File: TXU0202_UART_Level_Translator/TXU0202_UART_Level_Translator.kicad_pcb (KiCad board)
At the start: 2 copper layers, 7.6 x 10.2 mm, 5 parts, among them J1 3V_SIDE, J2 5V_SIDE, U1 TXU0202DCUR

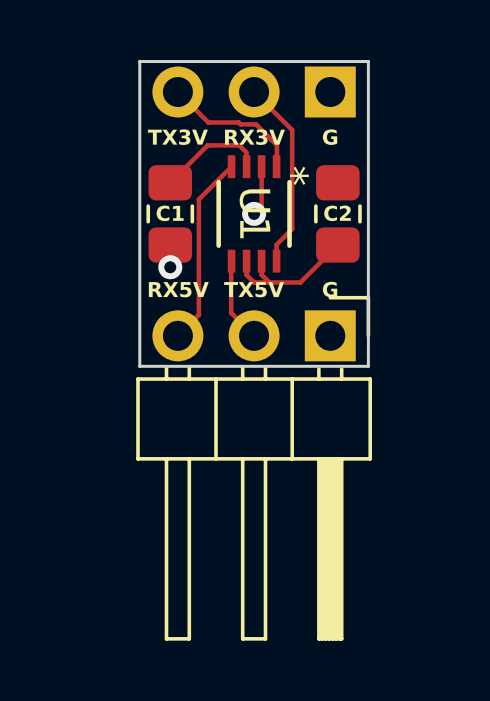
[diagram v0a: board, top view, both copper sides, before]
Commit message: adding a few mew projects, most recent is Sallen_Key_Stage v1.0
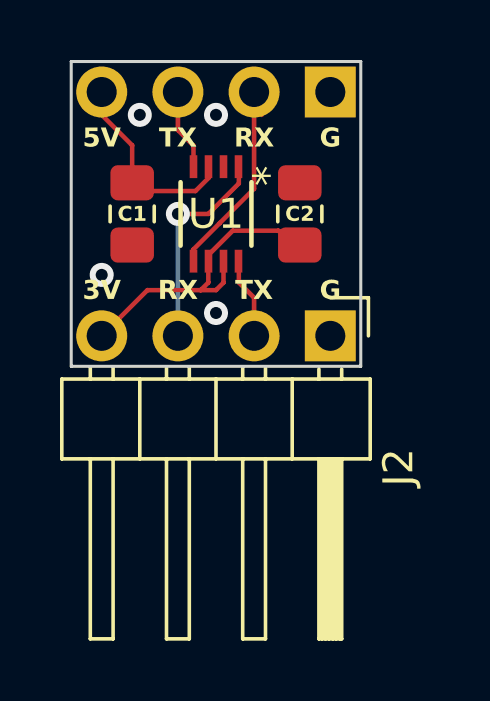
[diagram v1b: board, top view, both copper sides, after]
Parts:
- J1: value 3V_SIDE -> 5V_SIDE; footprint Connector_PinHeader_2.54mm:PinHeader_1x03_P2.54mm_Horizontal -> Connector_PinHeader_2.54mm:PinHeader_1x04_P2.54mm_Horizontal
- J2: value 5V_SIDE -> 3V_SIDE; footprint Connector_PinHeader_2.54mm:PinHeader_1x03_P2.54mm_Horizontal -> Connector_PinHeader_2.54mm:PinHeader_1x04_P2.54mm_Horizontal
- moved C2 1.27 mm to (99.3, 69.8)
- moved U1 1.27 mm to (96.5, 69.8)
- moved C1 1.27 mm to (93.7, 69.8)
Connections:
- J1 pad 2: /RX_3V -> /TX_5V
- J1 pad 3: /TX_3V -> /RX_5V
- J2 pad 2: /TX_5V -> /RX_3V
- J2 pad 3: /RX_5V -> /TX_3V
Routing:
- net +3.3V: track 4.74 -> 9.54 mm
- net /RX_5V: track 6.38 -> 1.94 mm
- net /TX_5V: track 2.86 -> 7.04 mm
- net /RX_3V: track 6.27 -> 2.50 mm
- net /TX_3V: track 4.55 -> 7.02 mm, vias 0 -> 1
- net GND: track 2.42 -> 0.00 mm, vias 2 -> 4
- net +5V: track 3.42 -> 5.53 mm
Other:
- board size 7.6 x 10.2 mm -> 9.7 x 10.2 mm
- board text added: "3V"
- board text added: "5V"
- board text added: "RX"
- board text added: "TX"
- board text added: "UART Level Shifter v1.1 JMiller"
- board text removed: "RX3V"
- board text removed: "RX5V"
- board text removed: "TX3V"
- board text removed: "TX5V"
